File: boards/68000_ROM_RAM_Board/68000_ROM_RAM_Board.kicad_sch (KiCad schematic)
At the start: 16 parts, among them J1 Conn_01x32, M1 RC2014_40_PIN, U1 74LS125, U3 W27C512, U4 AS6C4008-55PCN, U5 AS6C4008-55PCN, U6 W27C512, U8 74LS138, U9 74LS139

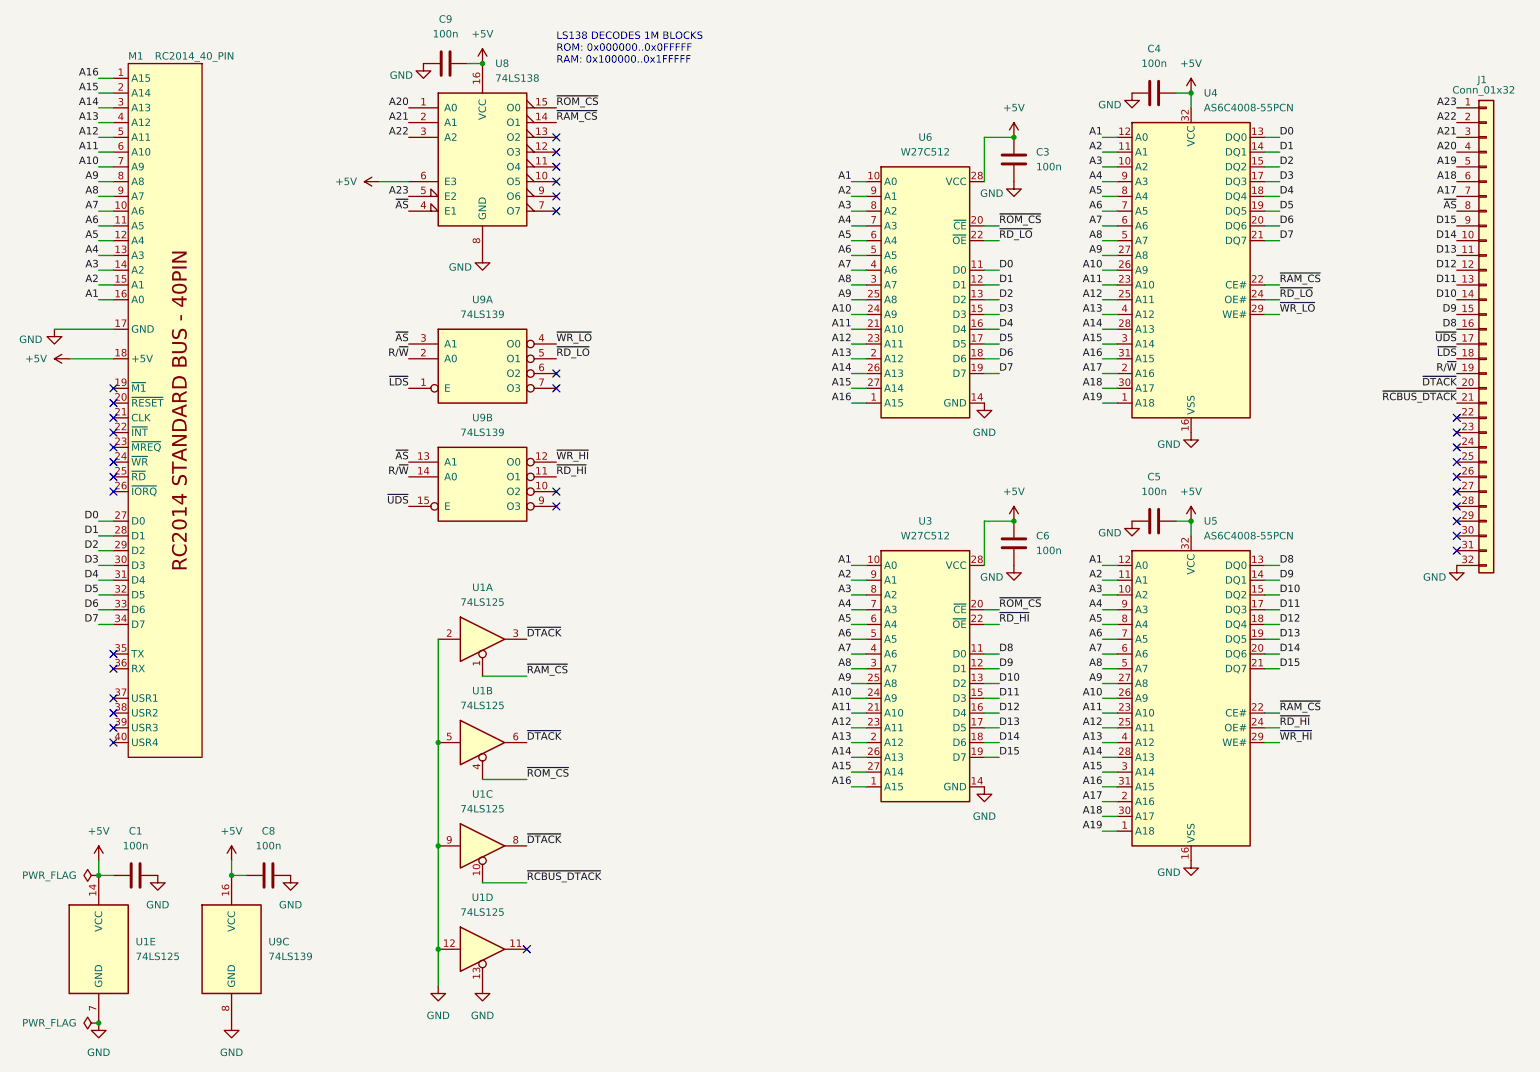
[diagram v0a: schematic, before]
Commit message: Update to v2 board set
Lots of updates to reflect the new v2 boards that use the full RCBus 80 pins as well as slight modifications to the various test programs to reflect the new IO and MEM space addresses.
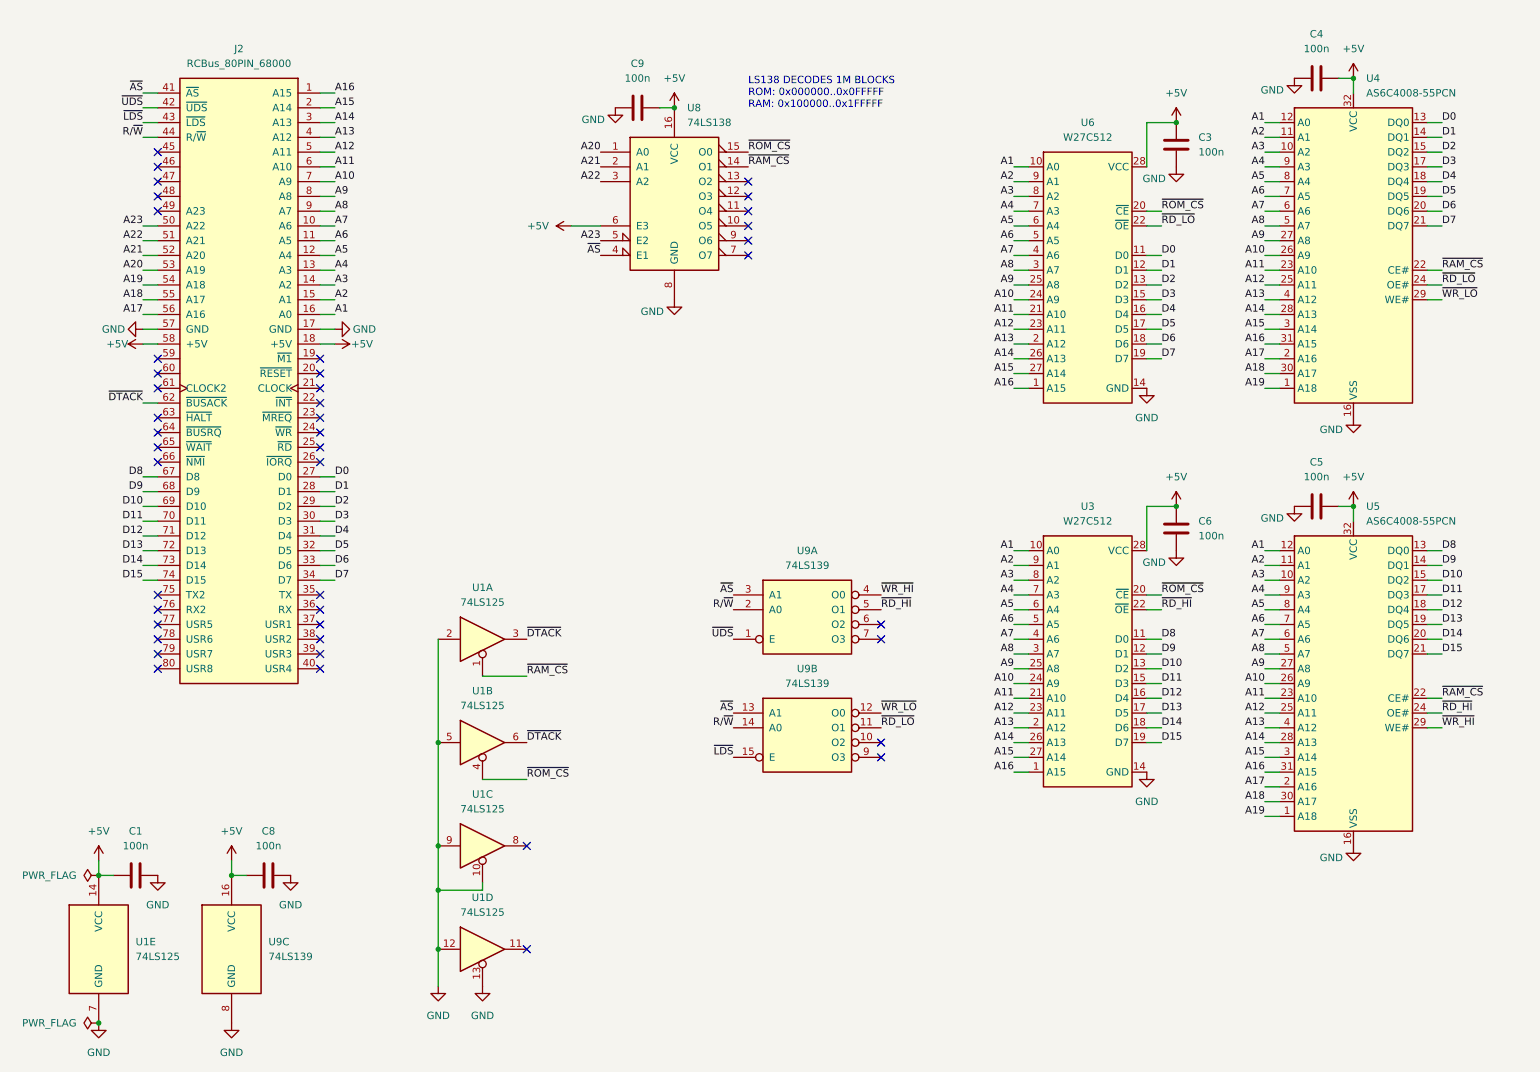
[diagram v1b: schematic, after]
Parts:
- removed J1: Conn_01x32, Connector_PinHeader_2.54mm:PinHeader_1x32_P2.54mm_Vertical, symbol Connector_Generic:Conn_01x32
- removed M1: RC2014_40_PIN, MyLibrary2023:RC2014_STD_40_PIN, symbol MyLibrary2023:RC2014_40_PIN
- added J2: RCBus_80PIN_68000, MyLibrary2023:RCBus_80p_Medium, symbol MyLibrary2023:RCBus_80PIN_68000
- U1: footprint Package_DIP:DIP-14_W7.62mm_Socket -> Package_DIP:DIP-14_W7.62mm
- U8, U9: footprint Package_DIP:DIP-16_W7.62mm_Socket -> Package_DIP:DIP-16_W7.62mm
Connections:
- net ~{RCBUS_DTACK} is gone; now on net GND: U1.10
- net +5V: now also J2.18 (+5V), J2.58 (+5V)
- net A1: now also J2.16 (A0)
- net A10: now also J2.7 (A9)
- net A11: now also J2.6 (A10)
- net A12: now also J2.5 (A11)
- net A13: now also J2.4 (A12)
- net A14: now also J2.3 (A13)
- net A15: now also J2.2 (A14)
- net A16: now also J2.1 (A15)
- net A17: now also J2.56 (A16)
- net A18: now also J2.55 (A17)
- net A19: now also J2.54 (A18)
- net A2: now also J2.15 (A1)
- net A20: now also J2.53 (A19)
- net A21: now also J2.52 (A20)
- net A22: now also J2.51 (A21)
- net A23: now also J2.50 (A22)
- net A3: now also J2.14 (A2)
- net A4: now also J2.13 (A3)
- net A5: now also J2.12 (A4)
- net A6: now also J2.11 (A5)
- net A7: now also J2.10 (A6)
- net A8: now also J2.9 (A7)
- net A9: now also J2.8 (A8)
- net D0: now also J2.27 (D0)
- net D1: now also J2.28 (D1)
- net D10: now also J2.69 (D10)
- net D11: now also J2.70 (D11)
- net D12: now also J2.71 (D12)
- net D13: now also J2.72 (D13)
- net D14: now also J2.73 (D14)
- net D15: now also J2.74 (D15)
- net D2: now also J2.29 (D2)
- net D3: now also J2.30 (D3)
- net D4: now also J2.31 (D4)
- net D5: now also J2.32 (D5)
- net D6: now also J2.33 (D6)
- net D7: now also J2.34 (D7)
- net D8: now also J2.67 (D8)
- net D9: now also J2.68 (D9)
- net GND: now also J2.17 (GND), J2.57 (GND)
- net R/~{W}: now also J2.44 (R/~{W})
- net ~{AS}: now also J2.41 (~{AS})
- net ~{DTACK}: now also J2.62 (~{BUSACK}); no longer U1.8
- net ~{LDS}: now also U9.15 (E), J2.43 (~{LDS}); no longer U9.1 (E)
- net ~{RD_HI}: now also U9.5 (O1); no longer U9.11 (O1)
- net ~{RD_LO}: now also U9.11 (O1); no longer U9.5 (O1)
- net ~{UDS}: now also U9.1 (E), J2.42 (~{UDS}); no longer U9.15 (E)
- net ~{WR_HI}: now also U9.4 (O0); no longer U9.12 (O0)
- net ~{WR_LO}: now also U9.12 (O0); no longer U9.4 (O0)
- no-connect marks 35 -> 44
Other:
- moved on the sheet: C3, C4, C5, C6, C9, U3, U4, U5, U6, U8, U9A, U9B
